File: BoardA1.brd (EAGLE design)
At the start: 44 x 100.5 mm, 20 parts, among them J1 LOAD_CELL1X03-PTH, J2 FEMALE 2x3, J3 LOAD_CELL1X03-PTH, J5 LOAD_CELL1X03-PTH, J6 LOAD_CELL1X03-PTH

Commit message: Merge branch 'master' of https://github.com/Luckycyq1010/SmartCrutch-ProtoBeta
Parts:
- moved J5 7.62 mm to (1.27, 91.4)
- moved J6 7.62 mm to (6.35, 87.6)
- moved J1 6.35 mm to (20.3, 90.2)
- moved J3 3.81 mm to (41.9, 90.2)
- moved R1 1.27 mm to (27.9, 85.1)
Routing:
- net -SIG1: track 21.5 -> 0.00 mm
- net -EX1: track 20.4 -> 0.12 mm
- net +EX2: track 41.1 -> 22.1 mm
- net -SIG2: track 24.5 -> 7.45 mm
- net +EX1: track 21.5 -> 6.35 mm
- net +SIG1: track 13.9 -> 0.00 mm
- net -EX2: track 23.2 -> 11.5 mm
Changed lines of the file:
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@@
 <plain>
 <wire x1="0" y1="0" x2="44" y2="0" width="0" layer="20"/>
-<wire x1="44" y1="0" x2="44" y2="100.5" width="0" layer="20"/>
+<wire x1="44" y1="93" x2="44" y2="100.5" width="0" layer="20"/>
 <wire x1="44" y1="100.5" x2="0" y2="100" width="0" layer="20"/>
-<wire x1="0" y1="100" x2="0" y2="0" width="0" layer="20"/>
-<hole x="2" y="3" drill="1"/>
-<hole x="40.64" y="3.81" drill="1"/>
-<hole x="42" y="97.5" drill="1"/>
-<hole x="2" y="97.5" drill="1"/>
+<wire x1="0" y1="100" x2="0" y2="93" width="0" layer="20"/>
 <dimension x1="0" y1="0" x2="44" y2="0" x3="22" y3="-3.81" textsize="1.778" layer="1"/>
 <dimension x1="44" y1="0" x2="44" y2="100.5" x3="48.26" y3="50.25" textsize="1.778" layer="1"/>
@@
 <element name="C3" library="SparkFun-Capacitors" package="0805" value="" x="16.51" y="58.42"/>
 <element name="C4" library="SparkFun-Capacitors" package="0805" value="" x="25.4" y="59.69"/>
-<element name="J1" library="Smartcrutches" package="1X03" value="LOAD_CELL1X03-PTH" x="26.67" y="90.17" rot="R180">
-<attribute name="SF_ID" value="SEN-10245" x="26.67" y="90.17" size="1.778" layer="27" rot="R180" display="off"/>
-</element>
-<element name="J3" library="Smartcrutches" package="1X03" value="LOAD_CELL1X03-PTH" x="38.1" y="90.17" rot="R180">
-<attribute name="SF_ID" value="SEN-10245" x="38.1" y="90.17" size="1.778" layer="27" rot="R180" display="off"/>
-</element>
-<element name="J5" library="Smartcrutches" package="1X03" value="LOAD_CELL1X03-PTH" x="8.89" y="91.44">
-<attribute name="SF_ID" value="SEN-10245" x="8.89" y="91.44" size="1.778" layer="27" display="off"/>
-</element>
-<element name="J6" library="Smartcrutches" package="1X03" value="LOAD_CELL1X03-PTH" x="13.97" y="87.63" rot="R180">
-<attribute name="SF_ID" value="SEN-10245" x="13.97" y="87.63" size="1.778" layer="27" rot="R180" display="off"/>
-</element>
-<element name="R1" library="eagle-ltspice" library_urn="urn:adsk.eagle:library:217" package="0204/7" value="" x="29.21" y="85.09" rot="R180">
-<attribute name="SPICEMODEL" value="NONE" x="29.21" y="85.09" size="1.778" layer="27" rot="R180" display="off"/>
-<attribute name="SPICEPREFIX" value="R" x="29.21" y="85.09" size="1.778" layer="27" rot="R180" display="off"/>
+<element name="J1" library="Smartcrutches" package="1X03" value="LOAD_CELL1X03-PTH" x="20.32" y="90.17" rot="R180">
+<attribute name="SF_ID" value="SEN-10245" x="20.32" y="90.17" size="1.778" layer="27" rot="R180" display="off"/>
+</element>
+<element name="J3" library="Smartcrutches" package="1X03" value="LOAD_CELL1X03-PTH" x="41.91" y="90.17" rot="R180">
+<attribute name="SF_ID" value="SEN-10245" x="41.91" y="90.17" size="1.778" layer="27" rot="R180" display="off"/>
+</element>
+<element name="J5" library="Smartcrutches" package="1X03" value="LOAD_CELL1X03-PTH" x="1.27" y="91.44">
+<attribute name="SF_ID" value="SEN-10245" x="1.27" y="91.44" size="1.778" layer="27" display="off"/>
+</element>
+<element name="J6" library="Smartcrutches" package="1X03" value="LOAD_CELL1X03-PTH" x="6.35" y="87.63" rot="R180">
+<attribute name="SF_ID" value="SEN-10245" x="6.35" y="87.63" size="1.778" layer="27" rot="R180" display="off"/>
+</element>
+<element name="R1" library="eagle-ltspice" library_urn="urn:adsk.eagle:library:217" package="0204/7" value="" x="27.94" y="85.09" rot="R180">
+<attribute name="SPICEMODEL" value="NONE" x="27.94" y="85.09" size="1.778" layer="27" rot="R180" display="off"/>
+<attribute name="SPICEPREFIX" value="R" x="27.94" y="85.09" size="1.778" layer="27" rot="R180" display="off"/>
 </element>
 <element name="R3" library="eagle-ltspice" library_urn="urn:adsk.eagle:library:217" package="0204/7" value="" x="30.48" y="87.63" rot="R180">
@@
 <contactref element="J3" pad="1"/>
 <wire x1="39.9288" y1="76.2" x2="40.02" y2="76.12" width="0.1524" layer="1"/>
-<wire x1="38.1" y1="90.17" x2="34.29" y2="87.63" width="0.1524" layer="16"/>
-<wire x1="36.3624" y1="79.6436875" x2="36.3624" y2="78.5963125" width="0.1524" layer="16"/>
-<wire x1="36.3624" y1="78.5963125" x2="36.4963125" y2="78.4624" width="0.1524" layer="16"/>
-<wire x1="34.29" y1="87.63" x2="34.29" y2="87.529475" width="0.1524" layer="16"/>
-<wire x1="37.6776" y1="78.4624" x2="40.02" y2="76.12" width="0.1524" layer="16"/>
-<wire x1="34.29" y1="87.529475" x2="37.6832" y2="84.136275" width="0.1524" layer="16"/>
-<wire x1="36.4963125" y1="78.4624" x2="37.6776" y2="78.4624" width="0.1524" layer="16"/>
-<wire x1="37.6832" y1="84.136275" x2="37.6832" y2="80.9644875" width="0.1524" layer="16"/>
-<wire x1="37.6832" y1="80.9644875" x2="36.3624" y2="79.6436875" width="0.1524" layer="16"/>
+<wire x1="34.29" y1="87.63" x2="41.91" y2="90.17" width="0" layer="19" extent="1-1"/>
+<wire x1="39.9288" y1="76.2" x2="34.29" y2="87.63" width="0" layer="19" extent="1-1"/>
 </signal>
 <signal name="-SIG1">
@@
 <contactref element="J3" pad="2"/>
 <contactref element="J1" pad="1"/>
-<wire x1="26.67" y1="90.17" x2="31.75" y2="91.44" width="0.1524" layer="1"/>
-<wire x1="31.75" y1="91.44" x2="35.56" y2="90.17" width="0.1524" layer="1"/>
-<wire x1="37.6832" y1="84.136275" x2="37.6832" y2="81.863725" width="0.1524" layer="1"/>
-<wire x1="35.56" y1="90.17" x2="35.56" y2="86.259475" width="0.1524" layer="1"/>
-<wire x1="37.6832" y1="81.863725" x2="37.02" y2="81.200525" width="0.1524" layer="1"/>
-<wire x1="37.02" y1="81.200525" x2="37.02" y2="79.12" width="0.1524" layer="1"/>
-<wire x1="35.56" y1="86.259475" x2="37.6832" y2="84.136275" width="0.1524" layer="1"/>
+<wire x1="37.02" y1="79.12" x2="39.37" y2="90.17" width="0" layer="19" extent="1-1"/>
+<wire x1="20.32" y1="90.17" x2="39.37" y2="90.17" width="0" layer="19" extent="1-1"/>
 </signal>
 <signal name="+SIG1">
@@
 <contactref element="R3" pad="2"/>
 <contactref element="R1" pad="1"/>
-<wire x1="30.02" y1="82.09" x2="30.02" y2="79.12" width="0.1524" layer="1"/>
-<wire x1="33.02" y1="85.09" x2="30.48" y2="82.55" width="0.1524" layer="1"/>
-<wire x1="30.48" y1="82.55" x2="30.02" y2="82.09" width="0.1524" layer="1"/>
-<wire x1="30.48" y1="82.55" x2="30.48" y2="83.82" width="0.1524" layer="1"/>
-<wire x1="30.48" y1="83.82" x2="26.67" y2="87.63" width="0.1524" layer="1"/>
+<wire x1="30.02" y1="79.12" x2="31.75" y2="85.09" width="0" layer="19" extent="1-1"/>
+<wire x1="26.67" y1="87.63" x2="31.75" y2="85.09" width="0" layer="19" extent="1-1"/>
 </signal>
 <signal name="+EX1">
@@
 <contactref element="J1" pad="2"/>
 <wire x1="27.02" y1="77.12" x2="27.02" y2="83.47" width="0.1524" layer="1"/>
-<wire x1="27.02" y1="83.47" x2="25.4" y2="85.09" width="0.1524" layer="1"/>
-<wire x1="25.4" y1="85.09" x2="25.4" y2="93.98" width="0.1524" layer="1"/>
-<wire x1="25.4" y1="93.98" x2="24.13" y2="90.17" width="0.1524" layer="1"/>
+<wire x1="27.02" y1="83.47" x2="24.13" y2="85.09" width="0" layer="19" extent="1-16"/>
+<wire x1="24.13" y1="85.09" x2="17.78" y2="90.17" width="0" layer="19" extent="1-1"/>
 </signal>
 <signal name="-EX2">
@@
 <wire x1="18.43" y1="76.12" x2="17.16" y2="76.85" width="0.1524" layer="1"/>
 <wire x1="17.16" y1="76.85" x2="22.86" y2="85.09" width="0.1524" layer="1"/>
-<wire x1="22.86" y1="85.09" x2="20.32" y2="82.55" width="0.1524" layer="1"/>
-<wire x1="20.32" y1="82.55" x2="13.97" y2="87.63" width="0.1524" layer="1"/>
+<wire x1="22.86" y1="85.09" x2="6.35" y2="87.63" width="0" layer="19" extent="1-1"/>
 </signal>
 <signal name="-SIG2">
@@
 <wire x1="15.43" y1="79.12" x2="14.16" y2="81.200525" width="0.1524" layer="16"/>
 <wire x1="14.16" y1="81.200525" x2="14.8232" y2="81.863725" width="0.1524" layer="16"/>
-<wire x1="14.8232" y1="85.9432" x2="11.43" y2="87.63" width="0.1524" layer="16"/>
+<wire x1="14.8232" y1="85.9432" x2="3.81" y2="87.63" width="0" layer="19" extent="1-16"/>
 <wire x1="14.8232" y1="81.863725" x2="14.8232" y2="85.9432" width="0.1524" layer="16"/>
-<wire x1="11.43" y1="87.63" x2="16.51" y2="88.9" width="0.1524" layer="16"/>
-<wire x1="16.51" y1="88.9" x2="8.89" y2="91.44" width="0.1524" layer="16"/>
+<wire x1="3.81" y1="87.63" x2="16.51" y2="88.9" width="0" layer="19" extent="1-16"/>
+<wire x1="16.51" y1="88.9" x2="1.27" y2="91.44" width="0" layer="19" extent="1-16"/>
 </signal>
 <signal name="+SIG2">
@@
 <wire x1="5.43" y1="77.12" x2="22.51" y2="77.12" width="0.1524" layer="16"/>
 <wire x1="22.51" y1="77.12" x2="25.4" y2="81.28" width="0.1524" layer="16"/>
-<wire x1="19.1516" y1="88.7984" x2="11.43" y2="91.44" width="0.1524" layer="16"/>
-<wire x1="25.4" y1="81.28" x2="25.4" y2="83.8072375" width="0.1524" layer="16"/>
-<wire x1="25.4" y1="83.8072375" x2="20.4088375" y2="88.7984" width="0.1524" layer="16"/>
-<wire x1="20.4088375" y1="88.7984" x2="19.1516" y2="88.7984" width="0.1524" layer="16"/>
+<wire x1="5.43" y1="77.12" x2="3.81" y2="91.44" width="0" layer="19" extent="1-1"/>
 </signal>
 <signal name="N$4">

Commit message: update
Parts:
- moved S1 12.8 mm to (30.5, 2.54)
- moved C1 10.9 mm to (25.4, 5.08)
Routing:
- net N$1: track 10.3 -> 28.3 mm
- net N$2: track 7.10 -> 17.9 mm
- net N$3: track 12.8 -> 12.1 mm
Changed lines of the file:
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@@
 </autorouter>
 <elements>
-<element name="C1" library="SparkFun-Capacitors" package="0805" value="" x="21.59" y="15.24"/>
+<element name="C1" library="SparkFun-Capacitors" package="0805" value="" x="25.4" y="5.08"/>
 <element name="C2" library="SparkFun-Capacitors" package="0805" value="" x="3.81" y="60.96" rot="R180"/>
 <element name="C3" library="SparkFun-Capacitors" package="0805" value="" x="16.51" y="58.42"/>
@@
 <attribute name="SPICEPREFIX" value="R" x="19.05" y="85.09" size="1.778" layer="27" rot="R180" display="off"/>
 </element>
-<element name="S1" library="SparkFun-Electromechanical" package="SWITCH-SPDT" value="" x="31.75" y="15.24" rot="R270">
-<attribute name="PROD_ID" value="SWCH-08261" x="31.75" y="15.24" size="1.778" layer="27" rot="R270" display="off"/>
+<element name="S1" library="SparkFun-Electromechanical" package="SWITCH-SPDT" value="" x="30.48" y="2.54" rot="R270">
+<attribute name="PROD_ID" value="SWCH-08261" x="30.48" y="2.54" size="1.778" layer="27" rot="R270" display="off"/>
 </element>
 <element name="U$1" library="Smartcrutches" package="DC-DCCONVERTER" value="" x="11.43" y="31.75" rot="R90"/>
@@
 <wire x1="20.574" y1="10.5156" x2="20.574" y2="15.24" width="0.1524" layer="1"/>
 <wire x1="19.05" y1="8.9916" x2="20.574" y2="10.5156" width="0.1524" layer="1"/>
-<wire x1="20.574" y1="15.24" x2="20.69" y2="15.24" width="0.1524" layer="1"/>
+<wire x1="20.574" y1="15.24" x2="24.5" y2="5.08" width="0.1524" layer="1"/>
 <wire x1="19.05" y1="8.9916" x2="19.05" y2="8.89" width="0.1524" layer="1"/>
 </signal>
@@
 <contactref element="U$1" pad="1"/>
 <wire x1="28.0416" y1="8.9916" x2="24.2316" y2="8.9916" width="0.1524" layer="1"/>
-<wire x1="34.29" y1="15.24" x2="28.0416" y2="8.9916" width="0.1524" layer="1"/>
+<wire x1="33.02" y1="2.54" x2="28.0416" y2="8.9916" width="0.1524" layer="1"/>
 <wire x1="24.2316" y1="8.9916" x2="24.13" y2="8.89" width="0.1524" layer="1"/>
 </signal>
@@
 <contactref element="C1" pad="2"/>
 <contactref element="S1" pad="2"/>
-<wire x1="27.432" y1="15.24" x2="22.49" y2="15.24" width="0.1524" layer="1"/>
+<wire x1="27.432" y1="15.24" x2="26.3" y2="5.08" width="0.1524" layer="1"/>
 <wire x1="28.6512" y1="16.4592" x2="27.432" y2="15.24" width="0.1524" layer="1"/>
 <wire x1="30.48" y1="16.4592" x2="28.6512" y2="16.4592" width="0.1524" layer="1"/>
 <wire x1="31.6992" y1="15.24" x2="30.48" y2="16.4592" width="0.1524" layer="1"/>
-<wire x1="31.6992" y1="15.24" x2="31.75" y2="15.24" width="0.1524" layer="1"/>
+<wire x1="31.6992" y1="15.24" x2="30.48" y2="2.54" width="0.1524" layer="1"/>
 </signal>
 <signal name="GND">

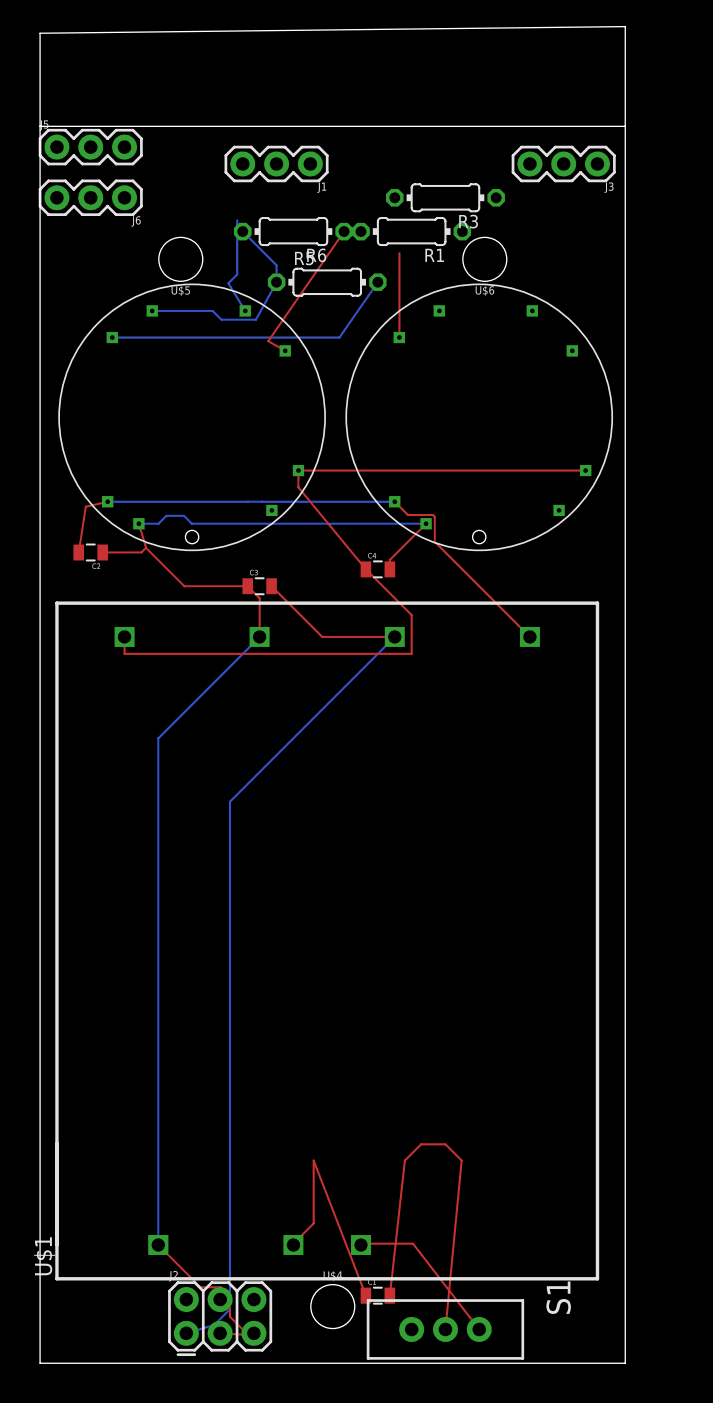
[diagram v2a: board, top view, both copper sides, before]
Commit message: made wire and vias thicker
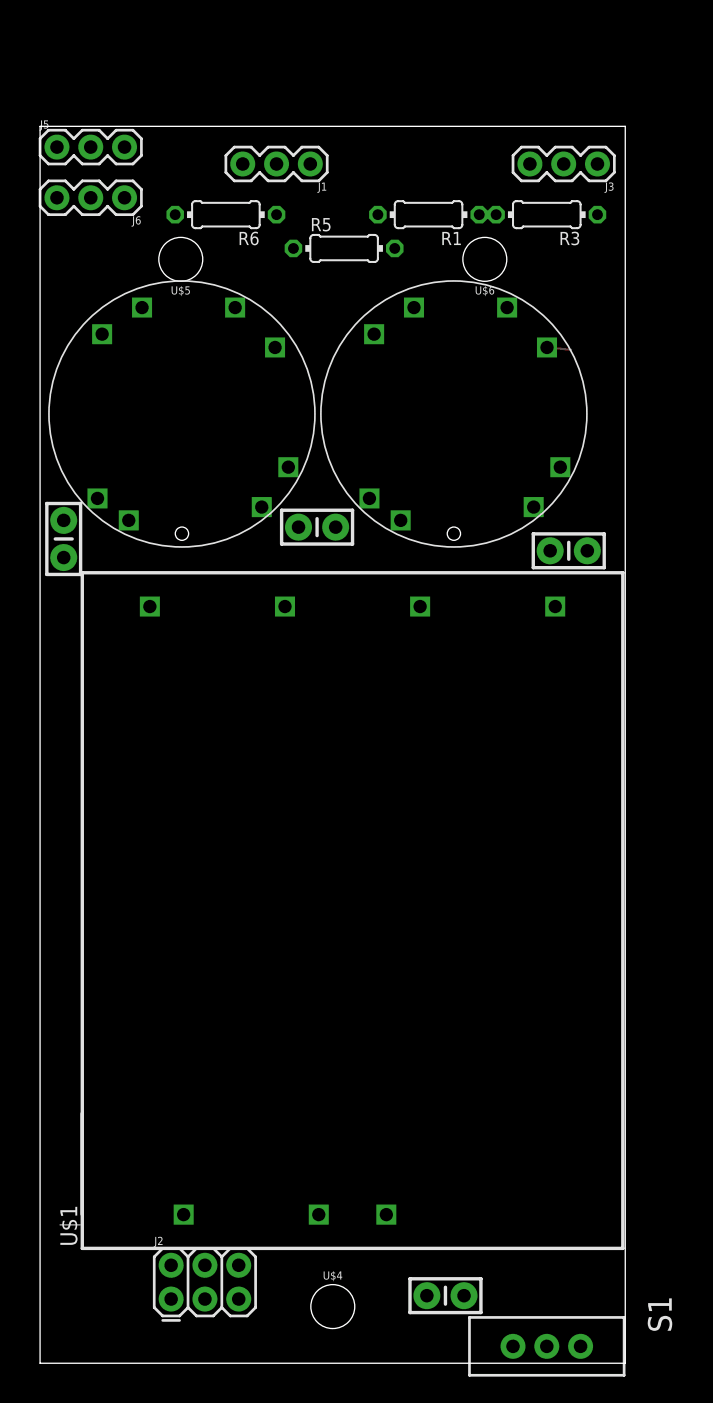
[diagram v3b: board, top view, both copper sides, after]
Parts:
- C1, C2, C3, C4: device SparkFun-Capacitors:0805 -> SparkFun-Capacitors:CAP-PTH-SMALL-KIT
- moved C4 14.4 mm to (39.8, 61.1)
- moved R3 7.73 mm to (38.1, 86.4)
- moved S1 7.73 mm to (38.1, 1.27)
- moved C3 6.20 mm to (20.8, 62.9)
- moved R6 5.24 mm to (14.0, 86.4)
- moved C1 5.08 mm to (30.5, 5.08)
- moved U$1 2.98 mm to (13.3, 34.0)
- moved R5 2.84 mm to (22.9, 83.8)
- moved J2 2.82 mm to (9.86, 4.83)
- moved C2 2.27 mm to (1.78, 62.0), turned to 270 degrees
- moved U$2 1.92 mm to (31.1, 71.4)
- moved R1 1.80 mm to (29.2, 86.4)
- moved U$3 0.80 mm to (10.7, 71.4)
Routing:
- net GND: track 106.4 -> 0.00 mm
- net 5V: track 70.4 -> 0.00 mm
- net -15V: track 61.5 -> 0.00 mm
- net +15V: track 42.2 -> 0.00 mm
- net N$1: track 28.3 -> 0.00 mm
- net +EX2: track 22.1 -> 0.00 mm
- net N$2: track 17.9 -> 0.00 mm
- net +SIG2: track 16.2 -> 0.00 mm
- net N$3: track 12.1 -> 0.00 mm
- net -EX2: track 11.5 -> 0.00 mm
- net -SIG2: track 7.45 -> 0.00 mm
- net +EX1: track 6.35 -> 0.00 mm
- net -EX1: track 0.12 -> 1.82 mm
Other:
- board size 44 x 100.5 mm -> 44 x 93 mm

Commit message: added connector
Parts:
- C1, C2, C3, C4: device SparkFun-Capacitors:CAP-PTH-SMALL-KIT -> SparkFun-Capacitors:0805
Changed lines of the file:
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@@
 </autorouter>
 <elements>
-<element name="C1" library="SparkFun-Capacitors" package="CAP-PTH-SMALL-KIT" value="" x="30.48" y="5.08"/>
-<element name="C2" library="SparkFun-Capacitors" package="CAP-PTH-SMALL-KIT" value="" x="1.778" y="61.976" rot="R270"/>
-<element name="C3" library="SparkFun-Capacitors" package="CAP-PTH-SMALL-KIT" value="" x="20.828" y="62.865"/>
-<element name="C4" library="SparkFun-Capacitors" package="CAP-PTH-SMALL-KIT" value="" x="39.751" y="61.087"/>
+<element name="C1" library="SparkFun-Capacitors" package="0805" value="" x="30.48" y="5.08"/>
+<element name="C2" library="SparkFun-Capacitors" package="0805" value="" x="1.778" y="61.976" rot="R270"/>
+<element name="C3" library="SparkFun-Capacitors" package="0805" value="" x="20.828" y="62.865"/>
+<element name="C4" library="SparkFun-Capacitors" package="0805" value="" x="39.751" y="61.087"/>
 <element name="J1" library="Smartcrutches" package="1X03" value="LOAD_CELL1X03-PTH" x="20.32" y="90.17" rot="R180">
 <attribute name="SF_ID" value="SEN-10245" x="20.32" y="90.17" size="1.778" layer="27" rot="R180" display="off"/>
@@
 <contactref element="C1" pad="1"/>
 <contactref element="U$1" pad="2"/>
-<wire x1="20.955" y1="11.176" x2="29.083" y2="5.08" width="0" layer="19" extent="1-1"/>
+<wire x1="20.955" y1="11.176" x2="29.58" y2="5.08" width="0" layer="19" extent="1-1"/>
 </signal>
 <signal name="N$3">
@@
 <contactref element="C1" pad="2"/>
 <contactref element="S1" pad="2"/>
-<wire x1="31.877" y1="5.08" x2="38.1" y2="1.27" width="0" layer="19" extent="1-1"/>
+<wire x1="31.38" y1="5.08" x2="38.1" y2="1.27" width="0" layer="19" extent="1-1"/>
 </signal>
 <signal name="GND">
@@
 <contactref element="C4" pad="2"/>
 <contactref element="J2" pad="3"/>
-<wire x1="41.148" y1="61.087" x2="27.115" y2="63.374" width="0" layer="19" extent="1-1"/>
-<wire x1="19.431" y1="62.865" x2="27.115" y2="63.374" width="0" layer="19" extent="1-1"/>
-<wire x1="18.415" y1="56.896" x2="19.431" y2="62.865" width="0" layer="19" extent="1-1"/>
-<wire x1="1.778" y1="63.373" x2="18.415" y2="56.896" width="0" layer="19" extent="1-1"/>
-<wire x1="6.668" y1="63.374" x2="1.778" y2="63.373" width="0" layer="19" extent="1-1"/>
+<wire x1="40.651" y1="61.087" x2="27.115" y2="63.374" width="0" layer="19" extent="1-1"/>
+<wire x1="19.928" y1="62.865" x2="27.115" y2="63.374" width="0" layer="19" extent="1-1"/>
+<wire x1="18.415" y1="56.896" x2="19.928" y2="62.865" width="0" layer="19" extent="1-1"/>
+<wire x1="1.778" y1="62.876" x2="18.415" y2="56.896" width="0" layer="19" extent="1-1"/>
+<wire x1="6.668" y1="63.374" x2="1.778" y2="62.876" width="0" layer="19" extent="1-1"/>
 <wire x1="10.795" y1="11.176" x2="18.415" y2="56.896" width="0" layer="19" extent="1-1"/>
 <wire x1="12.3952" y1="4.826" x2="10.795" y2="11.176" width="0" layer="19" extent="1-1"/>
@@
 <wire x1="24.765" y1="65.024" x2="38.735" y2="56.896" width="0" layer="19" extent="1-1"/>
 <wire x1="4.318" y1="65.024" x2="24.765" y2="65.024" width="0" layer="19" extent="1-1"/>
-<wire x1="1.778" y1="60.579" x2="4.318" y2="65.024" width="0" layer="19" extent="1-1"/>
+<wire x1="1.778" y1="61.076" x2="4.318" y2="65.024" width="0" layer="19" extent="1-1"/>
 </signal>
 <signal name="5V">
@@
 <contactref element="C3" pad="2"/>
 <contactref element="J2" pad="1"/>
-<wire x1="22.225" y1="62.865" x2="28.575" y2="56.896" width="0" layer="19" extent="1-1"/>
+<wire x1="21.728" y1="62.865" x2="28.575" y2="56.896" width="0" layer="19" extent="1-1"/>
 <wire x1="9.8552" y1="4.826" x2="28.575" y2="56.896" width="0" layer="19" extent="1-1"/>
 </signal>
@@
 <contactref element="U$2" pad="6"/>
 <contactref element="U$3" pad="6"/>
-<wire x1="38.354" y1="61.087" x2="39.115" y2="67.374" width="0" layer="19" extent="1-1"/>
-<wire x1="18.668" y1="67.374" x2="38.354" y2="61.087" width="0" layer="19" extent="1-1"/>
+<wire x1="38.851" y1="61.087" x2="39.115" y2="67.374" width="0" layer="19" extent="1-1"/>
+<wire x1="18.668" y1="67.374" x2="38.851" y2="61.087" width="0" layer="19" extent="1-1"/>
 <wire x1="8.255" y1="56.896" x2="18.668" y2="67.374" width="0" layer="19" extent="1-1"/>
 </signal>

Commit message: update 3
added battery connector
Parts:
- added LOADCELL: (no value), SparkFun-Connectors:2X4
- added LOWERLOADCELL: (no value), SparkFun-Connectors:1X05
- added MOTOR: (no value), SparkFun-Connectors:1X02
- C1, C2, C3, C4: device SparkFun-Capacitors:0805 -> SparkFun-Capacitors:CAP-PTH-SMALL-KIT
- moved J1 87.6 mm to (108.0, 90.2)
- moved J3 61.8 mm to (102.9, 80.0)
- moved J6 50.0 mm to (-34.3, 58.4)
- moved J5 43.4 mm to (-39.4, 76.2)
- moved C1 3.70 mm to (27.3, 6.99)
- moved S1 0.40 mm to (38.2, 0.89)
